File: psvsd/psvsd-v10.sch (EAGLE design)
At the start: 28 parts, among them J1 TRANSFLASH-PUSH, U1 USB2244QFN, U3 VREG, Y1 24.000MHz

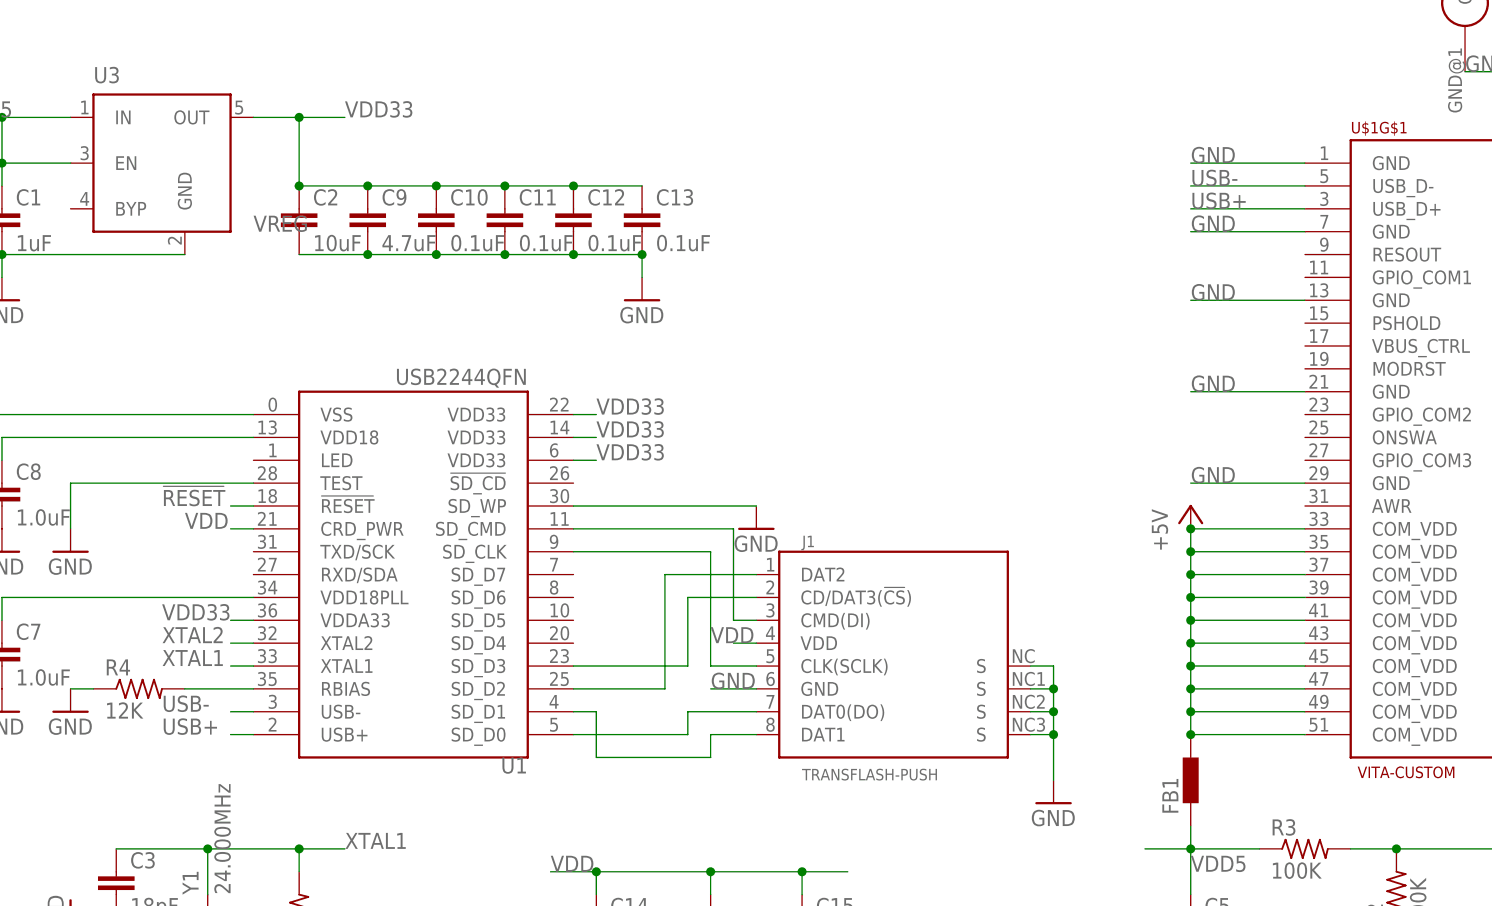
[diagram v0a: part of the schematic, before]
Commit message: Fixed USB+/USB- signal in psvsd
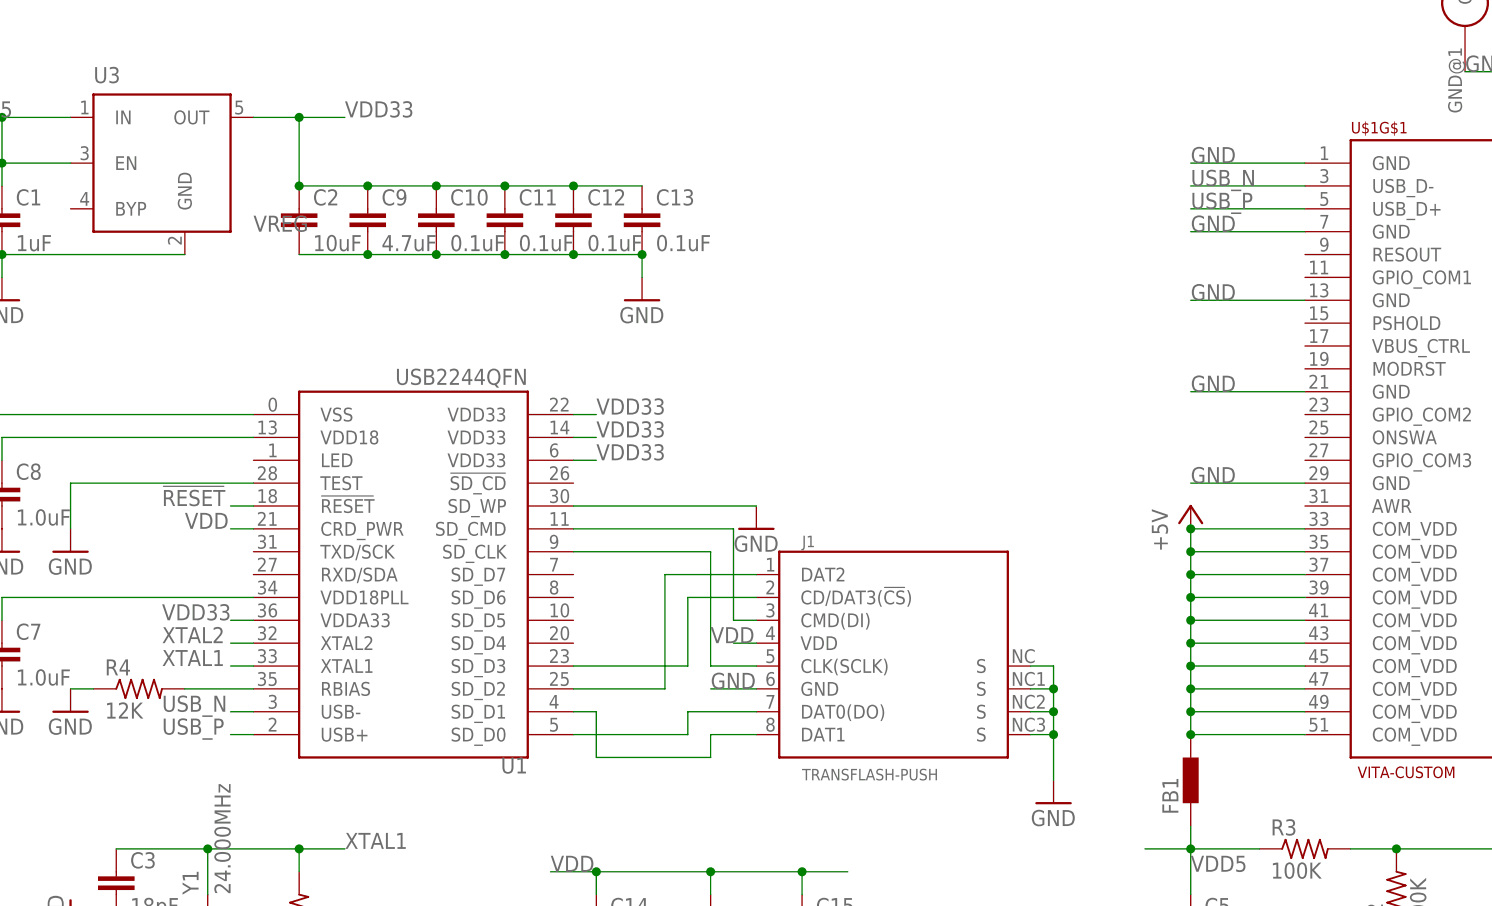
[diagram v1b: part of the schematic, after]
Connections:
- net USB+ renamed USB_P
- net USB- renamed USB_N
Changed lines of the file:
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@@
 </segment>
 </net>
-<net name="USB-" class="0">
+<net name="USB_N" class="0">
 <segment>
 <pinref part="U1" gate="G$1" pin="USB-"/>
@@
 </segment>
 </net>
-<net name="USB+" class="0">
+<net name="USB_P" class="0">
 <segment>
 <pinref part="U1" gate="G$1" pin="USB+"/>

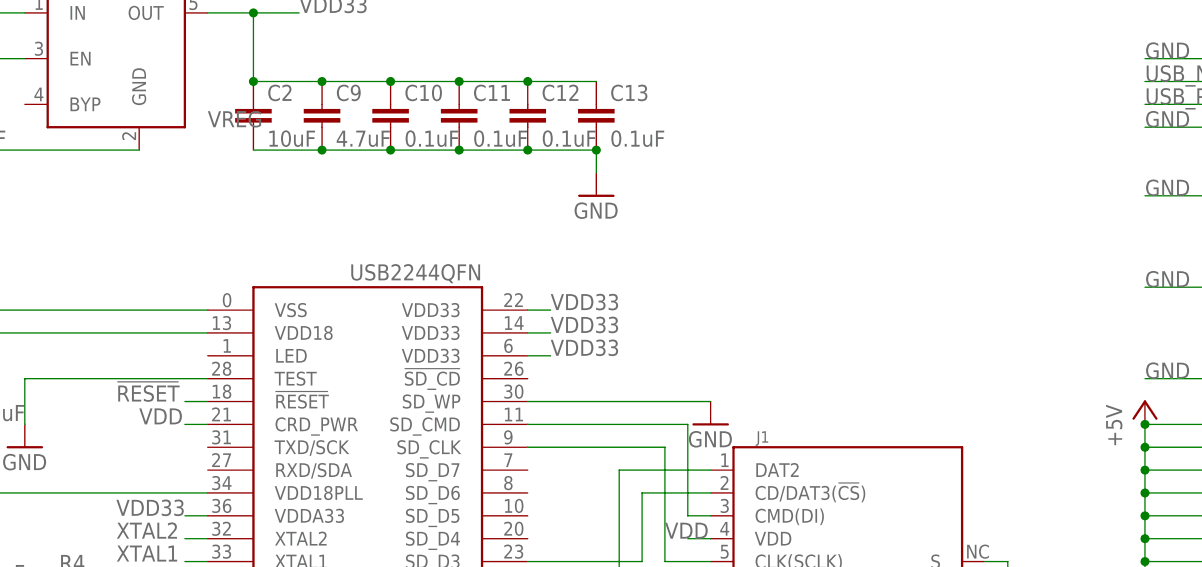
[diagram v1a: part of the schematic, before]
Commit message: Added LED indicator
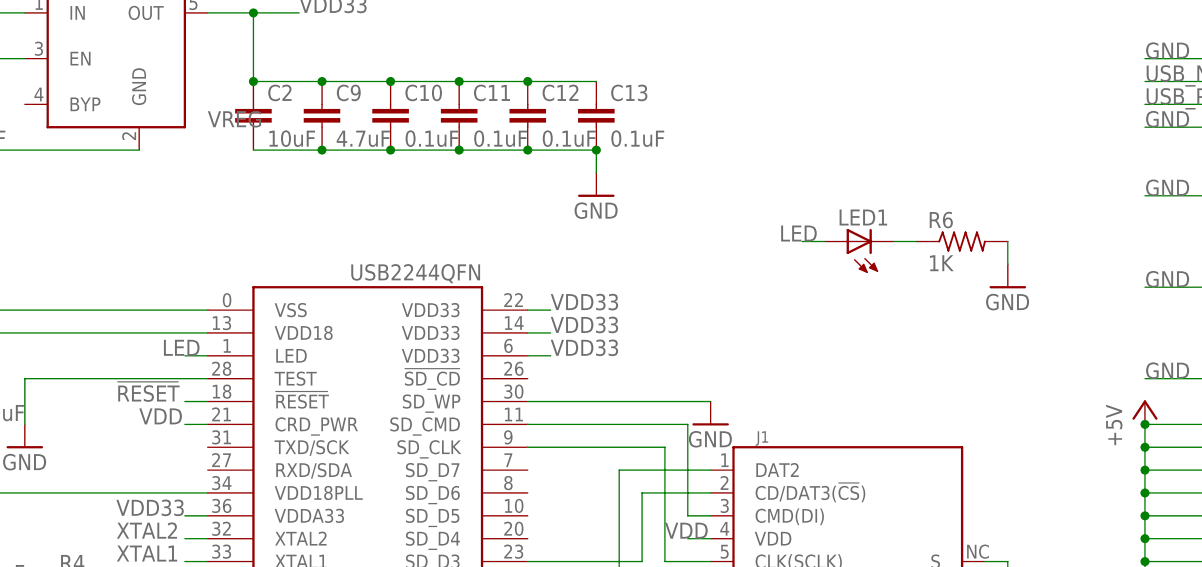
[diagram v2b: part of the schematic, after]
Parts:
- added LED1: (no value), led:LEDSML0603
- added R6: 1K, rcl:R-US_R0603
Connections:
- new net LED: LED1.A, U1.LED
- new net N$1: LED1.C, R6.1
- net GND: now also R6.2
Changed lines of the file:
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@@
 <part name="GND3" library="supply1" deviceset="GND" device=""/>
 <part name="GND14" library="supply1" deviceset="GND" device=""/>
+<part name="LED1" library="led" deviceset="LED" device="SML0603"/>
+<part name="R6" library="rcl" deviceset="R-US_" device="R0603" value="1K"/>
+<part name="GND15" library="supply1" deviceset="GND" device=""/>
 </parts>
 <sheets>
@@
 <instance part="GND3" gate="1" x="-170.18" y="-48.26" rot="R270"/>
 <instance part="GND14" gate="1" x="-60.96" y="-35.56"/>
+<instance part="LED1" gate="G$1" x="-78.74" y="15.24" rot="R90"/>
+<instance part="R6" gate="G$1" x="-66.04" y="15.24"/>
+<instance part="GND15" gate="1" x="-60.96" y="10.16"/>
 </instances>
 <busses>
@@
 <junction x="-60.96" y="-27.94"/>
 <pinref part="GND14" gate="1" pin="GND"/>
+</segment>
+<segment>
+<pinref part="R6" gate="G$1" pin="2"/>
+<pinref part="GND15" gate="1" pin="GND"/>
+<wire x1="-60.96" y1="15.24" x2="-60.96" y2="12.7" width="0.1524" layer="91"/>
 </segment>
 </net>
@@
 </segment>
 </net>
+<net name="N$1" class="0">
+<segment>
+<pinref part="LED1" gate="G$1" pin="C"/>
+<pinref part="R6" gate="G$1" pin="1"/>
+<wire x1="-73.66" y1="15.24" x2="-71.12" y2="15.24" width="0.1524" layer="91"/>
+</segment>
+</net>
+<net name="LED" class="0">
+<segment>
+<pinref part="U1" gate="G$1" pin="LED"/>
+<wire x1="-149.86" y1="2.54" x2="-152.4" y2="2.54" width="0.1524" layer="91"/>
+<label x="-154.94" y="2.54" size="1.778" layer="95"/>
+</segment>
+<segment>
+<pinref part="LED1" gate="G$1" pin="A"/>
+<wire x1="-81.28" y1="15.24" x2="-83.82" y2="15.24" width="0.1524" layer="91"/>
+<label x="-86.36" y="15.24" size="1.778" layer="95"/>
+</segment>
+</net>

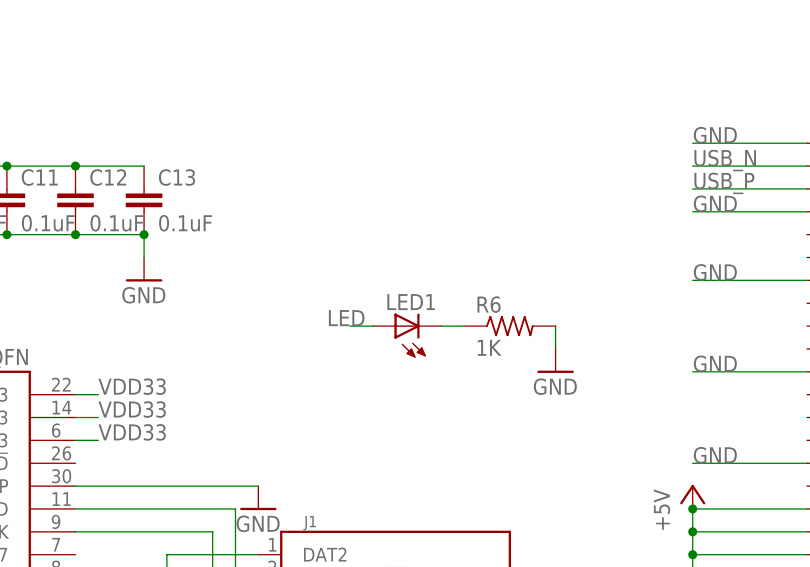
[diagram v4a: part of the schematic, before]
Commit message: Added value for LED
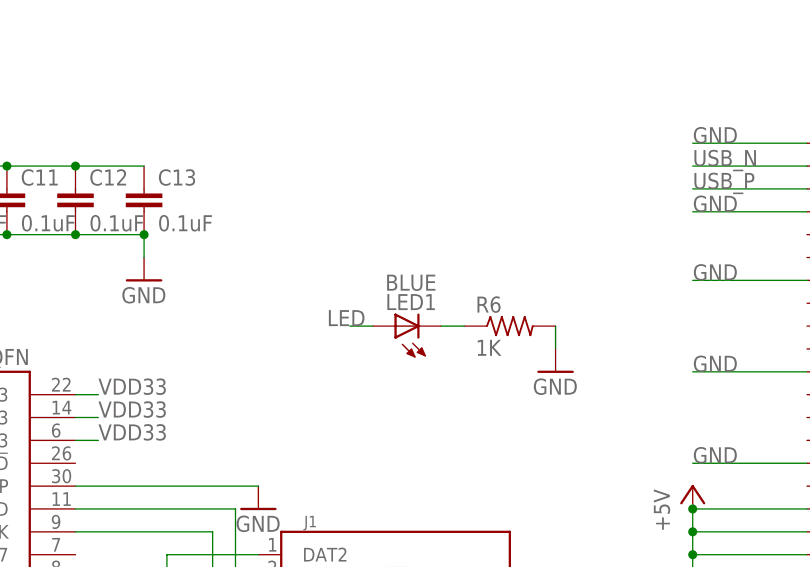
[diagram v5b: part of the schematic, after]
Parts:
- LED1: value (none) -> BLUE
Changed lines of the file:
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@@
 <part name="GND3" library="supply1" deviceset="GND" device=""/>
 <part name="GND14" library="supply1" deviceset="GND" device=""/>
-<part name="LED1" library="led" deviceset="LED" device="SML0603"/>
+<part name="LED1" library="led" deviceset="LED" device="SML0603" value="BLUE"/>
 <part name="R6" library="rcl" deviceset="R-US_" device="R0603" value="1K"/>
 <part name="GND15" library="supply1" deviceset="GND" device=""/>

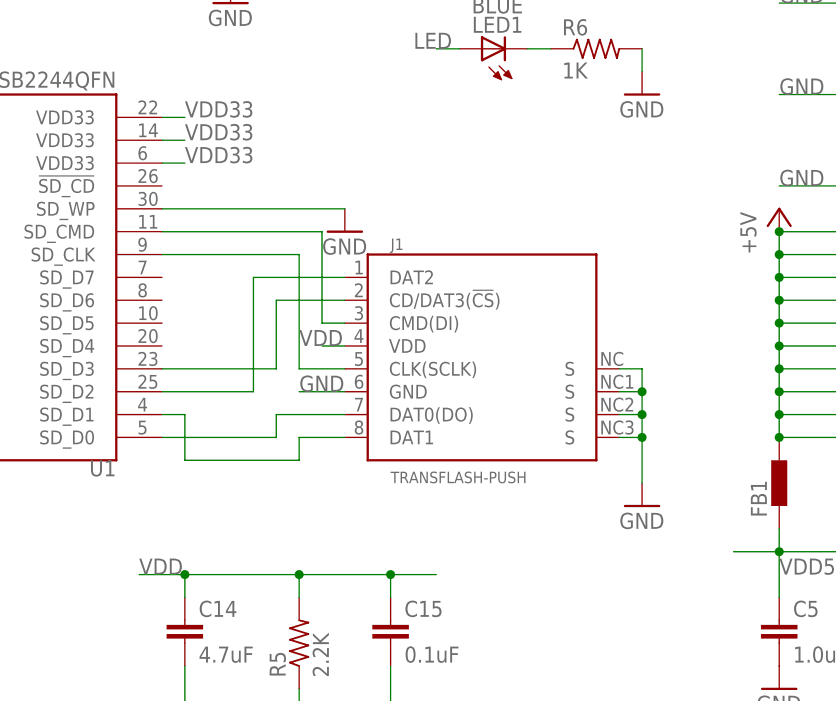
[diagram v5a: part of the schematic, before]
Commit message: Added MEM2051 part that will be used
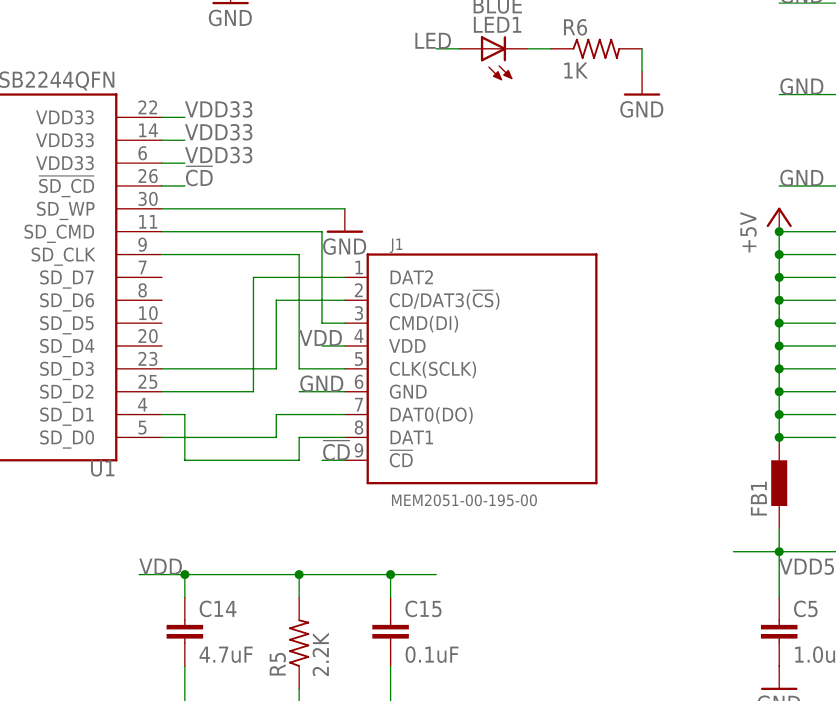
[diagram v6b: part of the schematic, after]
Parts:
- J1: value TRANSFLASH-PUSH -> MEM2051-00-195-00; device sd-mmc:TRANSFLASH-PUSH -> sd-mmc:MEM2051-00-195-00
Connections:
- new net !CD: J1.!CD, U1.!SD_CD
- net GND: no longer J1.S@1, J1.S@2, J1.S@3, J1.S@4
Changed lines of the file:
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@@
 <?xml version="1.0" encoding="utf-8"?>
 <!DOCTYPE eagle SYSTEM "eagle.dtd">
-<eagle version="8.1.1">
+<eagle version="8.2.0">
 <drawing>
 <settings>
@@
 <part name="GND" library="supply1" deviceset="GND" device=""/>
 <part name="P+1" library="supply1" deviceset="+5V" device=""/>
-<part name="J1" library="sd-mmc" deviceset="TRANSFLASH" device="-PUSH"/>
+<part name="J1" library="sd-mmc" deviceset="MEM2051" device="-00-195-00"/>
 <part name="U1" library="USB2244" deviceset="USB2244" device="QFN"/>
 <part name="JP1" library="pinhead" deviceset="PINHD-1X5" device="" value="UART_KERMIT"/>
@@
 <part name="GND13" library="supply1" deviceset="GND" device=""/>
 <part name="GND3" library="supply1" deviceset="GND" device=""/>
-<part name="GND14" library="supply1" deviceset="GND" device=""/>
 <part name="LED1" library="led" deviceset="LED" device="SML0603" value="BLUE"/>
 <part name="R6" library="rcl" deviceset="R-US_" device="R0603" value="1K"/>
@@
 <instance part="GND13" gate="1" x="-93.98" y="-5.08"/>
 <instance part="GND3" gate="1" x="-170.18" y="-48.26" rot="R270"/>
-<instance part="GND14" gate="1" x="-60.96" y="-35.56"/>
 <instance part="LED1" gate="G$1" x="-78.74" y="15.24" rot="R90"/>
 <instance part="R6" gate="G$1" x="-66.04" y="15.24"/>
@@
 <junction x="-165.1" y="-48.26"/>
 <pinref part="GND3" gate="1" pin="GND"/>
-</segment>
-<segment>
-<pinref part="J1" gate="G$1" pin="S@1"/>
-<wire x1="-63.5" y1="-20.32" x2="-60.96" y2="-20.32" width="0.1524" layer="91"/>
-<wire x1="-60.96" y1="-20.32" x2="-60.96" y2="-22.86" width="0.1524" layer="91"/>
-<pinref part="J1" gate="G$1" pin="S@2"/>
-<wire x1="-60.96" y1="-22.86" x2="-60.96" y2="-25.4" width="0.1524" layer="91"/>
-<wire x1="-60.96" y1="-25.4" x2="-60.96" y2="-27.94" width="0.1524" layer="91"/>
-<wire x1="-60.96" y1="-27.94" x2="-60.96" y2="-33.02" width="0.1524" layer="91"/>
-<wire x1="-63.5" y1="-22.86" x2="-60.96" y2="-22.86" width="0.1524" layer="91"/>
-<junction x="-60.96" y="-22.86"/>
-<pinref part="J1" gate="G$1" pin="S@3"/>
-<wire x1="-63.5" y1="-25.4" x2="-60.96" y2="-25.4" width="0.1524" layer="91"/>
-<junction x="-60.96" y="-25.4"/>
-<pinref part="J1" gate="G$1" pin="S@4"/>
-<wire x1="-63.5" y1="-27.94" x2="-60.96" y2="-27.94" width="0.1524" layer="91"/>
-<junction x="-60.96" y="-27.94"/>
-<pinref part="GND14" gate="1" pin="GND"/>
 </segment>
 <segment>
@@
 </segment>
 </net>
+<net name="!CD" class="0">
+<segment>
+<pinref part="U1" gate="G$1" pin="!SD_CD"/>
+<wire x1="-114.3" y1="0" x2="-111.76" y2="0" width="0.1524" layer="91"/>
+<label x="-111.76" y="0" size="1.778" layer="95"/>
+</segment>
+<segment>
+<pinref part="J1" gate="G$1" pin="!CD"/>
+<wire x1="-93.98" y1="-30.48" x2="-96.52" y2="-30.48" width="0.1524" layer="91"/>
+<label x="-96.52" y="-30.48" size="1.778" layer="95"/>
+</segment>
+</net>

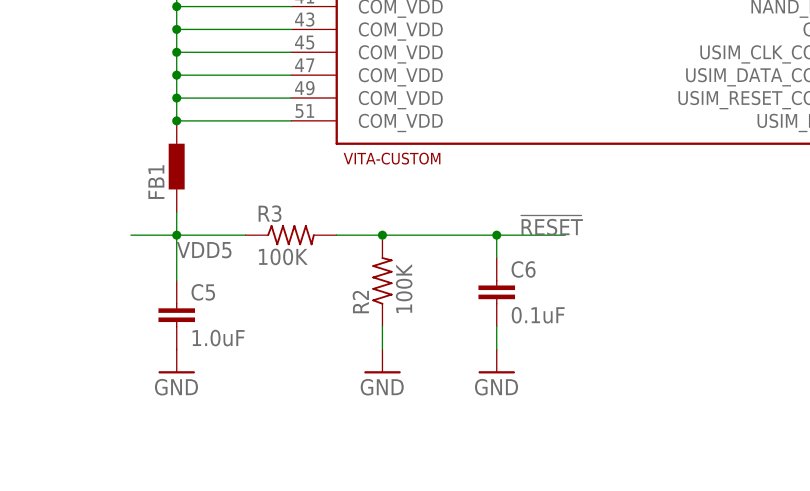
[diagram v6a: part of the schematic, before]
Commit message: Changed RC circuit for reset to be tolerant of 4.0V
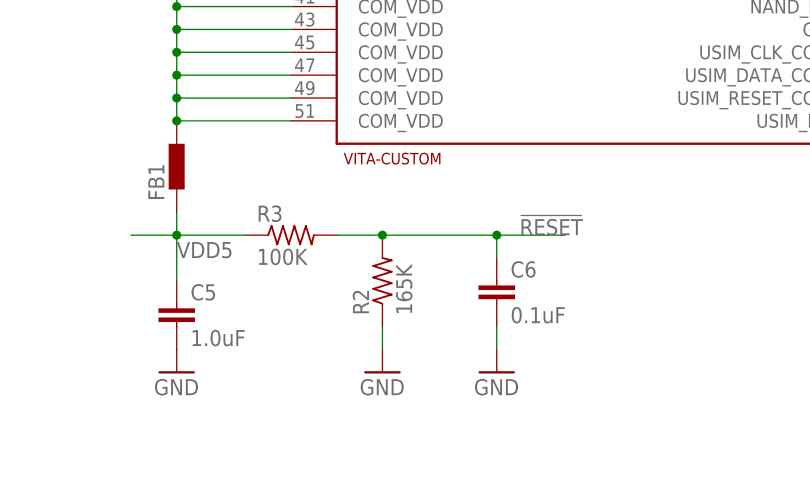
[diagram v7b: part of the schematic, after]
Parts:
- R2: value 100K -> 165K
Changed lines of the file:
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@@
 <part name="FB1" library="inductors" deviceset="BLM15H" device="" technology="B121SN1" value=""/>
 <part name="C5" library="rcl" deviceset="C-EU" device="C0603" value="1.0uF"/>
-<part name="R2" library="rcl" deviceset="R-US_" device="R0603" value="100K"/>
+<part name="R2" library="rcl" deviceset="R-US_" device="R0603" value="165K"/>
 <part name="C6" library="rcl" deviceset="C-EU" device="C0402" value="0.1uF"/>
 <part name="R3" library="rcl" deviceset="R-US_" device="R0603" value="100K"/>
